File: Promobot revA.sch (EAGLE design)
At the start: 450 parts, among them J3 USB-MICRO!!!, J4 3x2M, M1OUTA MOUNTINGHOLE2.5_THICK, M1OUTA1 MOUNTINGHOLE2.5_THICK, M1OUTA10 MOUNTINGHOLE2.5_THICK, M1OUTA11 MOUNTINGHOLE2.5_THICK, M1OUTA12 MOUNTINGHOLE2.5_THICK, M1OUTA13 MOUNTINGHOLE2.5_THICK, M1OUTA14 MOUNTINGHOLE2.5_THICK, M1OUTA15 MOUNTINGHOLE2.5_THICK, M1OUTA16 MOUNTINGHOLE2.5_THICK, M1OUTA17 MOUNTINGHOLE2.5_THICK, M1OUTA18 MOUNTINGHOLE2.5_THICK, M1OUTA19 MOUNTINGHOLE2.5_THICK, M1OUTA2 MOUNTINGHOLE2.5_THICK, M1OUTA20 MOUNTINGHOLE2.5_THICK, M1OUTA21 MOUNTINGHOLE2.5_THICK, M1OUTA22 MOUNTINGHOLE2.5_THICK, M1OUTA23 MOUNTINGHOLE2.5_THICK, M1OUTA24 MOUNTINGHOLE2.5_THICK, M1OUTA25 MOUNTINGHOLE2.5_THICK, M1OUTA3 MOUNTINGHOLE2.5_THICK, M1OUTA4 MOUNTINGHOLE2.5_THICK, M1OUTA5 MOUNTINGHOLE2.5_THICK, M1OUTA6 MOUNTINGHOLE2.5_THICK, M1OUTA7 MOUNTINGHOLE2.5_THICK, M1OUTA8 MOUNTINGHOLE2.5_THICK, M1OUTA9 MOUNTINGHOLE2.5_THICK, M1OUTB MOUNTINGHOLE2.5_THICK, M1OUTB1 MOUNTINGHOLE2.5_THICK, M1OUTB2 MOUNTINGHOLE2.5_THICK, M1OUTB3 MOUNTINGHOLE2.5_THICK, M1OUTB4 MOUNTINGHOLE2.5_THICK, M1OUTB5 MOUNTINGHOLE2.5_THICK, Q1 IPB80N03S4L-03, Q2 IPB80N03S4L-03, Q3 IPB80N03S4L-03, Q4 IPB80N03S4L-03, Q6 CSD86330Q3D, Q7 CSD86330Q3D, T1 FDN340P/PMV48XP, T2 PMV48XP, U1 VNH5019A-E, U10 ATMEGA32U4-XUMU, U11 NCP1117-5, U12 TPS563200, U2 ACS714, U3 VNH5019A-E, U4 ACS714, U5 VNH5019A-E, U6 ACS714, U7 VNH5019A-E, U8 ACS714, U9 LP2985-33DBVR, X1 MKS1852-6-0-202, X10 MKS1852-6-0-202, X11 MKS1852-6-0-202, X12 MKS1852-6-0-202, X13 MKS1852-6-0-202, X14 MKS1852-6-0-202, X15 MKS1852-6-0-202, X16 MKS1852-6-0-202, X17 MKS1852-6-0-202, X18 MKS1852-6-0-202, X19 MKS1852-6-0-202, X2 MKS1852-6-0-202, X20 MKS1852-6-0-202, X21 MKS1852-6-0-202, X22 MKS1852-6-0-202, X23 MKS1852-6-0-202, X24 MKS1852-6-0-202, X3 RC-5231, X4 RC-5231, X5 MKS1852-6-0-202, X6 MKS1852-6-0-202, X7 MKS1852-6-0-202, X8 MKS1852-6-0-202, X9 MKS1852-6-0-202, Y3 16MHz KX-7

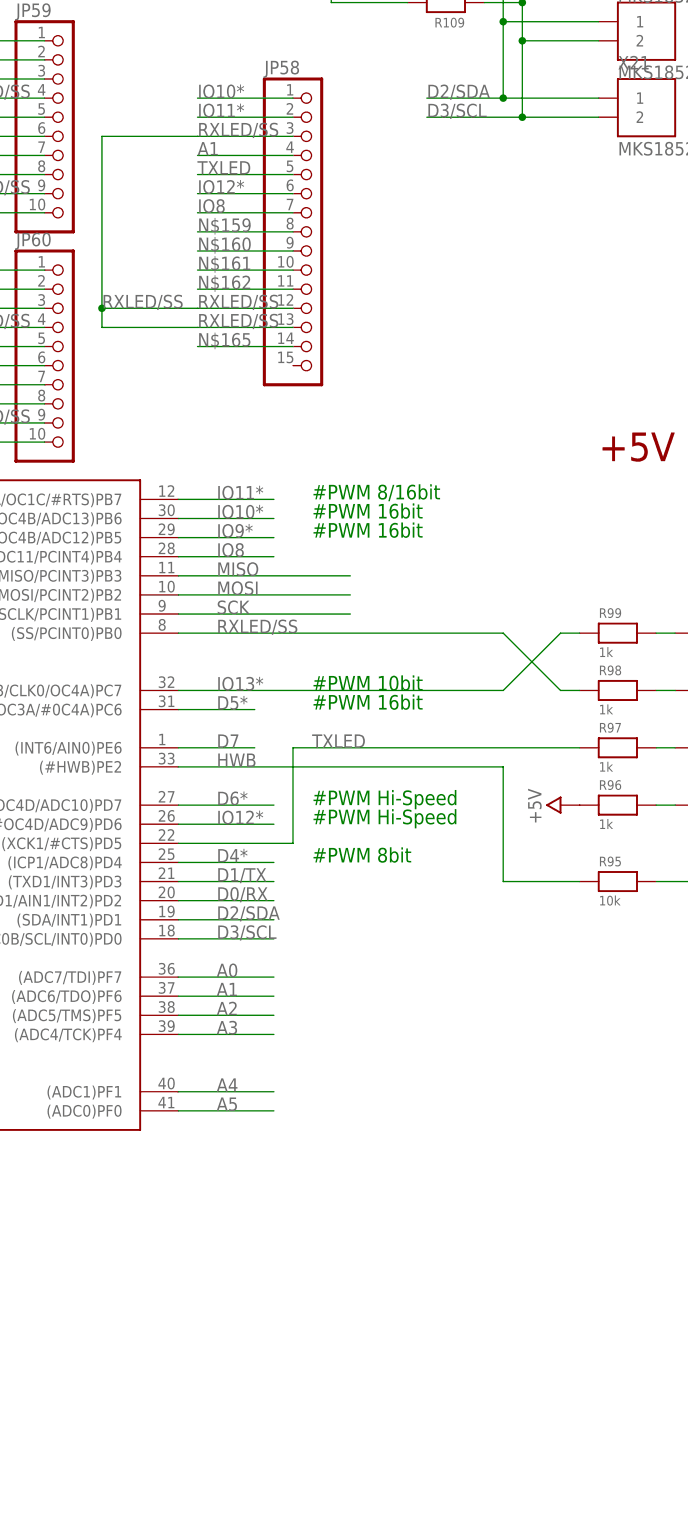
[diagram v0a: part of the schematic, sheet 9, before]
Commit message: Add voltage divider
R110, R111 - voltage divider. Connected to A5 pin
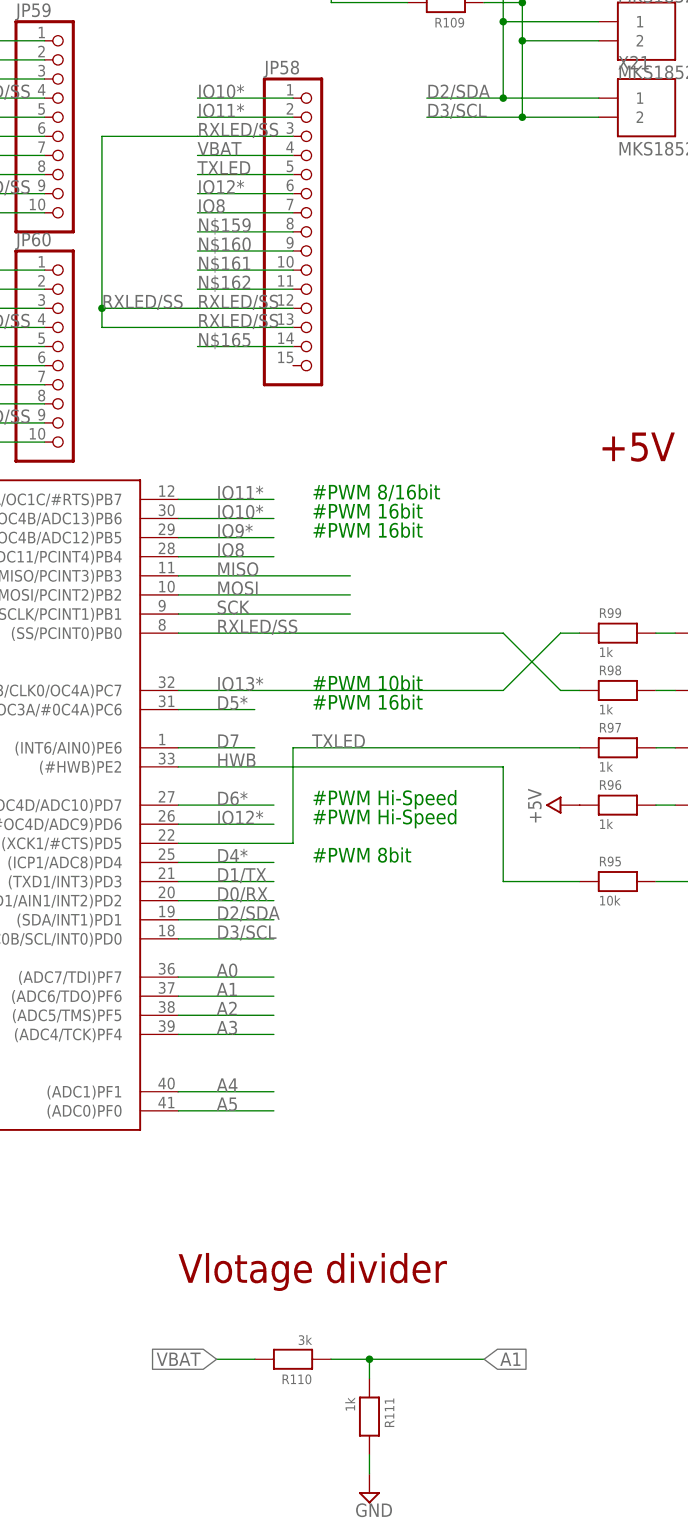
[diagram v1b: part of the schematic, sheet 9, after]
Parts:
- added R110: 3k, microbuilder:RESISTOR_0603MP
- added R111: 1k, microbuilder:RESISTOR_0603MP
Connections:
- removed net N$99: JP40.1, JP47.1
- new net VBAT: JP58.4, R110.2
- net A1: now also R110.1, R111.1; no longer JP58.4
- net GND: now also R111.2
- net MAINVCC: now also JP47.1
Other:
- note added: "Vlotage divider"
